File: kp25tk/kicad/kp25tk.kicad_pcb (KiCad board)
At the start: 2 copper layers, 100 x 138.4 mm, 99 parts, among them J1 Host Connector, J2 Config Header, J3 Power In, J4 Row Select In, J5 Column Out, J6 NMI Out, J7 Reset Out, J8 Switch, SW0 KEY00, SW1 KEY01, SW10 KEY0A, SW11 KEY0B, SW12 KEY0C, SW13 KEY0D, SW14 KEY0E, SW15 KEY0F, SW16 KEY10, SW17 KEY11, SW18 KEY12, SW19 KEY13, SW2 KEY02, SW20 KEY14, SW21 KEY15, SW22 KEY16, SW23 KEY17, SW24 NMI, SW25 RESET, SW27 SWITCH, SW3 KEY03, SW4 KEY04, SW5 KEY05, SW6 KEY06, SW7 KEY07, SW8 KEY08, SW9 KEY09, U1 74LS14

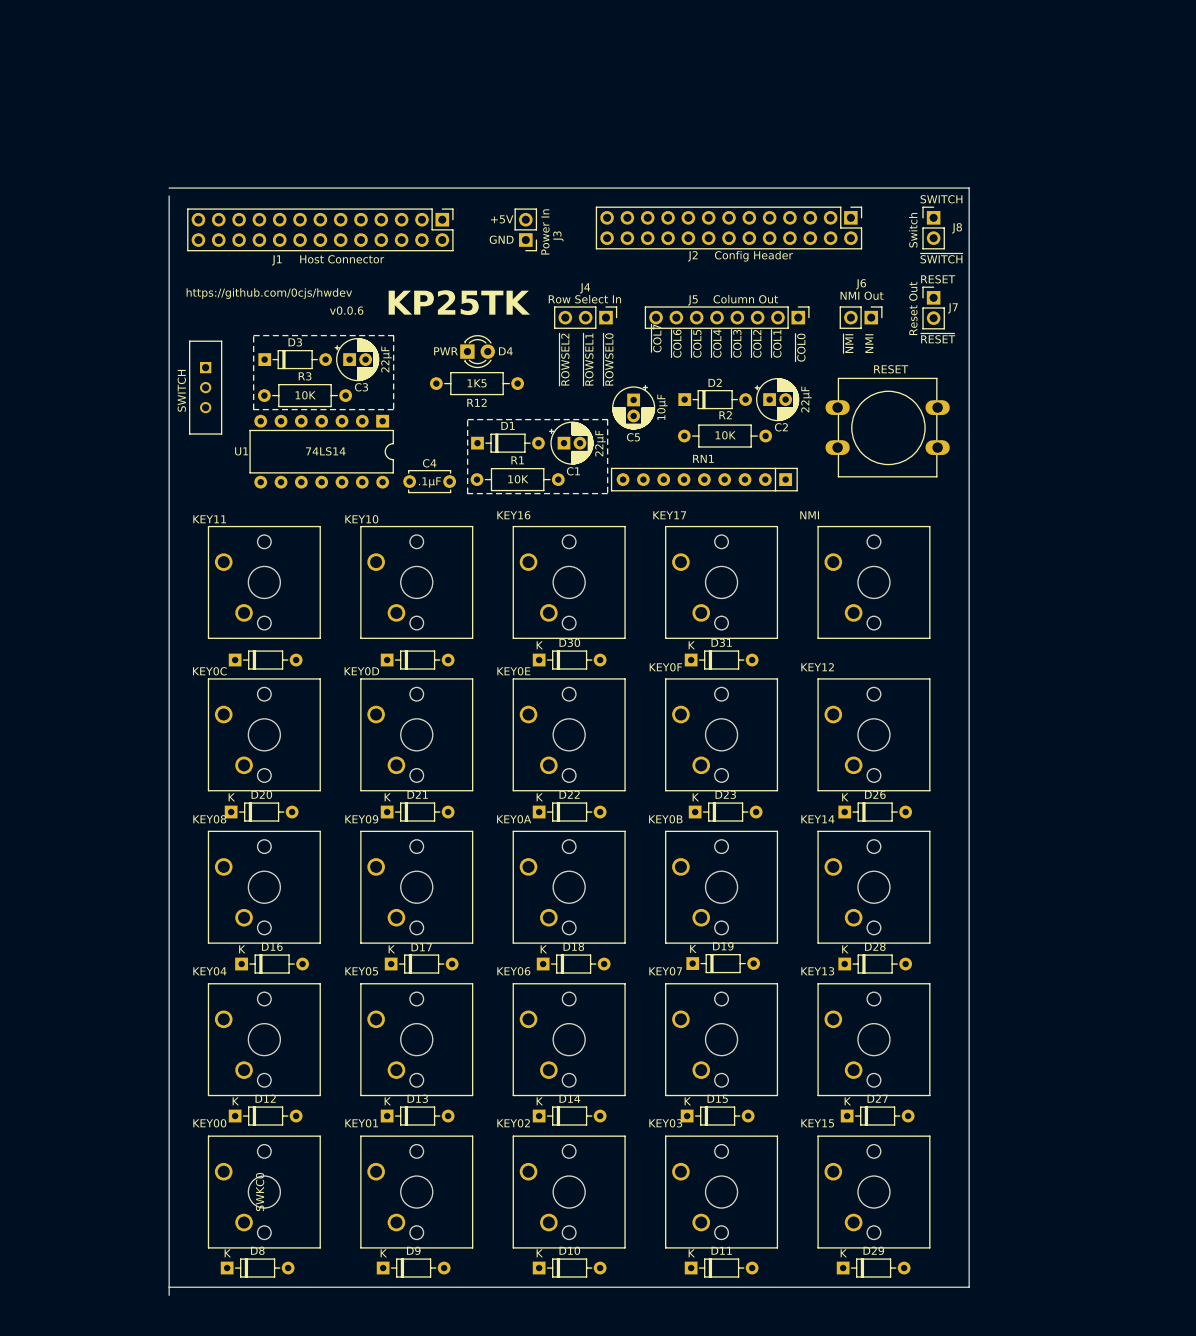
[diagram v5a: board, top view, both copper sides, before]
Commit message: kp25tk/: Schematic cleaned up and ready for peer review; more board layout
Board bumped to 0.0.7 to match schematic. Schematic stays there because
it had such minor changes.
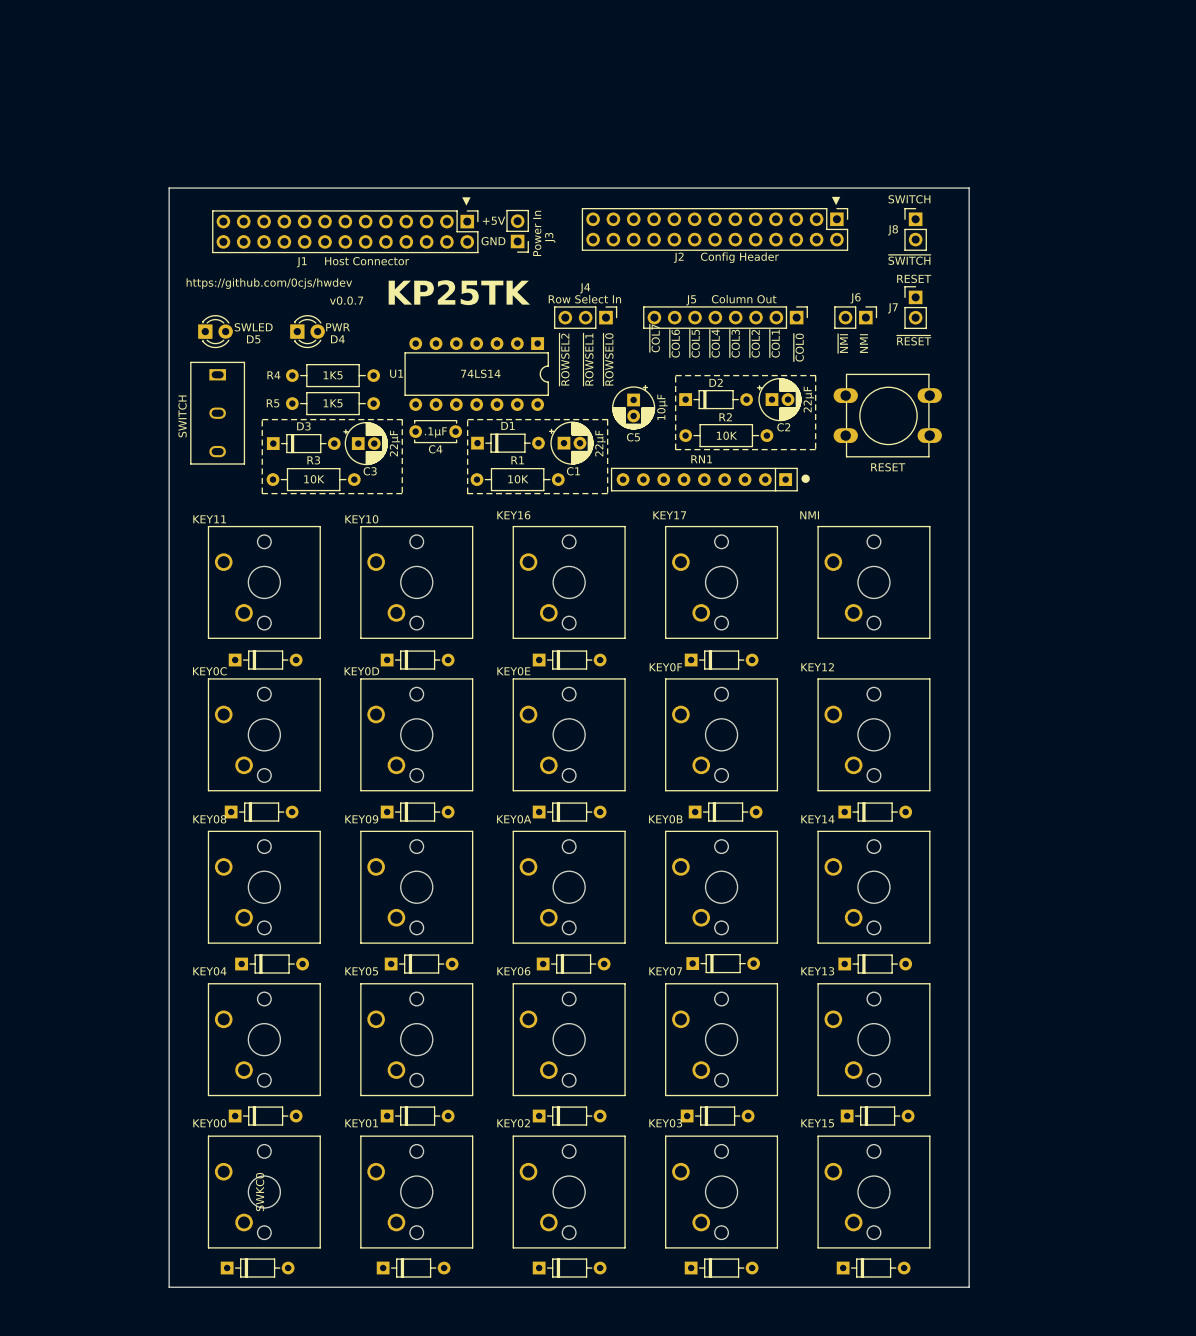
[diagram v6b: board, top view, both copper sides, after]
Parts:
- added D5: SWLED, LED_THT:LED_D3.0mm, F.Cu at (49.2, 63.5)
- added R5: 1K5, Resistor_THT:R_Axial_DIN0207_L6.3mm_D2.5mm_P10.16mm_Horizontal, F.Cu at (70.3, 72.5)
- D4: value LED -> PWR
- moved R4 28.2 mm to (60.1, 69.0), turned to 0 degrees
- moved U1 21.7 mm to (90.8, 65.0)
- moved D4 21.4 mm to (60.7, 63.5)
- moved C3 10.6 mm to (68.4, 77.5)
- moved D3 10.6 mm to (57.7, 77.5)
- moved R3 10.6 mm to (57.7, 82.0)
- moved R2 10.0 mm to (109.3, 76.5), turned to 0 degrees
- moved C4 7.56 mm to (75.5, 76.0), turned to 0 degrees
- moved SW27 3.53 mm to (50.8, 73.7)
- moved J1 3.13 mm to (82.0, 49.8)
- moved J8 2.26 mm to (138.0, 49.5)
- moved J7 2.25 mm to (138.0, 59.2)
- moved J2 1.76 mm to (128.2, 49.5)
- moved SW25 1.50 mm to (128.3, 71.5)
- moved J3 1.04 mm to (88.3, 52.2)
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- renumbered R12 to R4
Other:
- board size 100 x 138.4 mm -> 100 x 137.4 mm

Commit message: kp25tk/: Release candidate 1
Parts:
- added ?: , , F.Cu at (47.4, 86.2)
- added ?: , , F.Cu at (47.4, 180.3)
- added ?: , , F.Cu at (47.4, 48.2)
- added ?: , , F.Cu at (142.1, 48.2)
- added ?: , , F.Cu at (142.1, 86.2)
- added ?: , , F.Cu at (142.1, 180.3)
- U1: value 74LS14 -> 74HLS14
- moved D8 1.19 mm to (53.2, 180.5)
- moved J1 1.10 mm to (83.1, 49.7)
- moved J3 0.90 mm to (89.2, 52.2)
- moved J8 0.75 mm to (137.3, 49.5)
- moved J7 0.75 mm to (137.3, 59.2)
- moved D15 0.69 mm to (110.2, 161.6)
- moved D20 0.69 mm to (53.2, 123.6)
- moved D16 0.62 mm to (53.2, 142.6)
- moved J6 0.55 mm to (131.3, 61.8)
- moved D9 0.44 mm to (71.9, 180.5)
- moved J5 0.38 mm to (122.8, 61.8)
- moved D27 0.31 mm to (129.2, 161.6)
- moved D17 0.31 mm to (72.2, 142.6)
- moved D18 0.31 mm to (91.2, 142.6)
- moved D23 0.31 mm to (110.2, 123.6)
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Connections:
- D5 pad 1: Net-(D5-K) -> Net-(D3-A)
- J8 pad 2: Net-(D5-K) -> Net-(J8-~{SWITCH})
- U1 pad 10: Net-(D5-K) -> Net-(J8-~{SWITCH})
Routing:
- net Net-(D10-K): track 0.00 -> 299.2 mm, vias 0 -> 1
- net Net-(D16-K): track 0.00 -> 255.0 mm, vias 0 -> 1
- net Net-(D24-K): track 0.00 -> 248.4 mm, vias 0 -> 1
- net Net-(J5-~{COL4}): track 0.00 -> 214.3 mm
- net Net-(J5-~{COL5}): track 0.00 -> 184.9 mm, vias 0 -> 1
- net Net-(J5-~{COL1}): track 0.00 -> 177.7 mm
- net Net-(J5-~{COL0}): track 0.00 -> 171.6 mm, vias 0 -> 1
- net Earth: track 0.00 -> 169.9 mm, vias 0 -> 29
- net Net-(J5-~{COL2}): track 0.00 -> 151.5 mm, vias 0 -> 1
- net +5V: track 0.00 -> 141.4 mm, vias 0 -> 4
- net Net-(J5-~{COL3}): track 0.00 -> 129.8 mm, vias 0 -> 1
- net Net-(J5-~{COL6}): track 0.00 -> 100.7 mm, vias 0 -> 1
- net Net-(J5-~{COL7}): track 0.00 -> 94.2 mm
- net /HOST15: track 0.00 -> 84.9 mm, vias 0 -> 1
- net /HOST13: track 0.00 -> 79.4 mm, vias 0 -> 1
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- added copper zone on B.Cu, net Earth
- added copper zone on F.Cu, net Earth
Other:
- outline, holes or cut-outs redrawn
